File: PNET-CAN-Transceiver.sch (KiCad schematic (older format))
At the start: 14 parts, among them J301 Termination, J302 PNET, J303 PNET, U301 LM358, U302 TCAN332DR

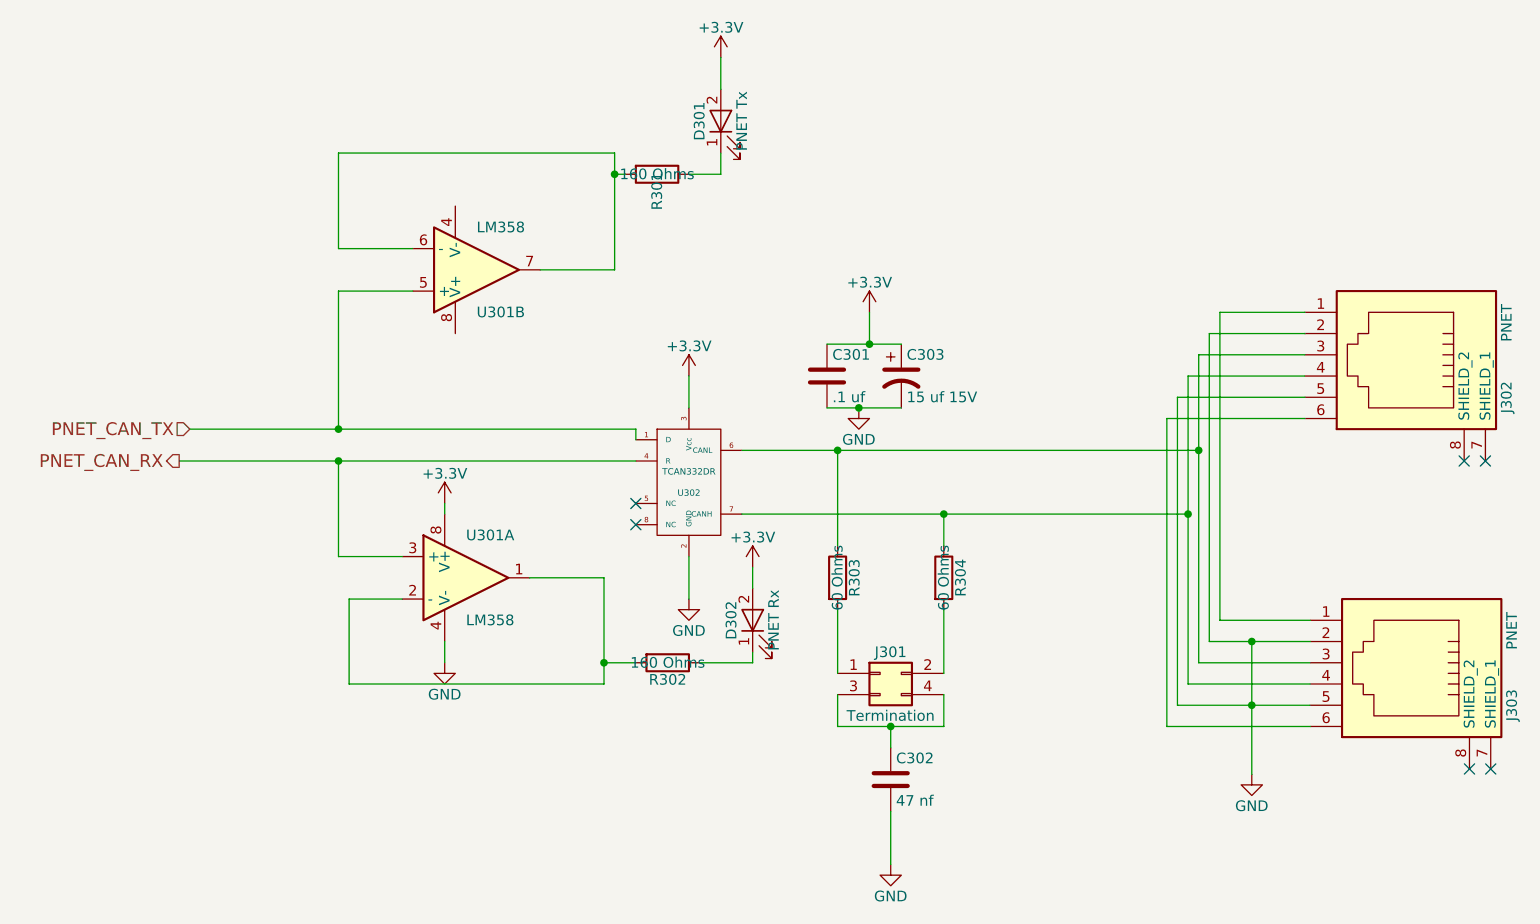
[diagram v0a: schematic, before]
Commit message: Correct for CAN Polarity on the PNET connectors.
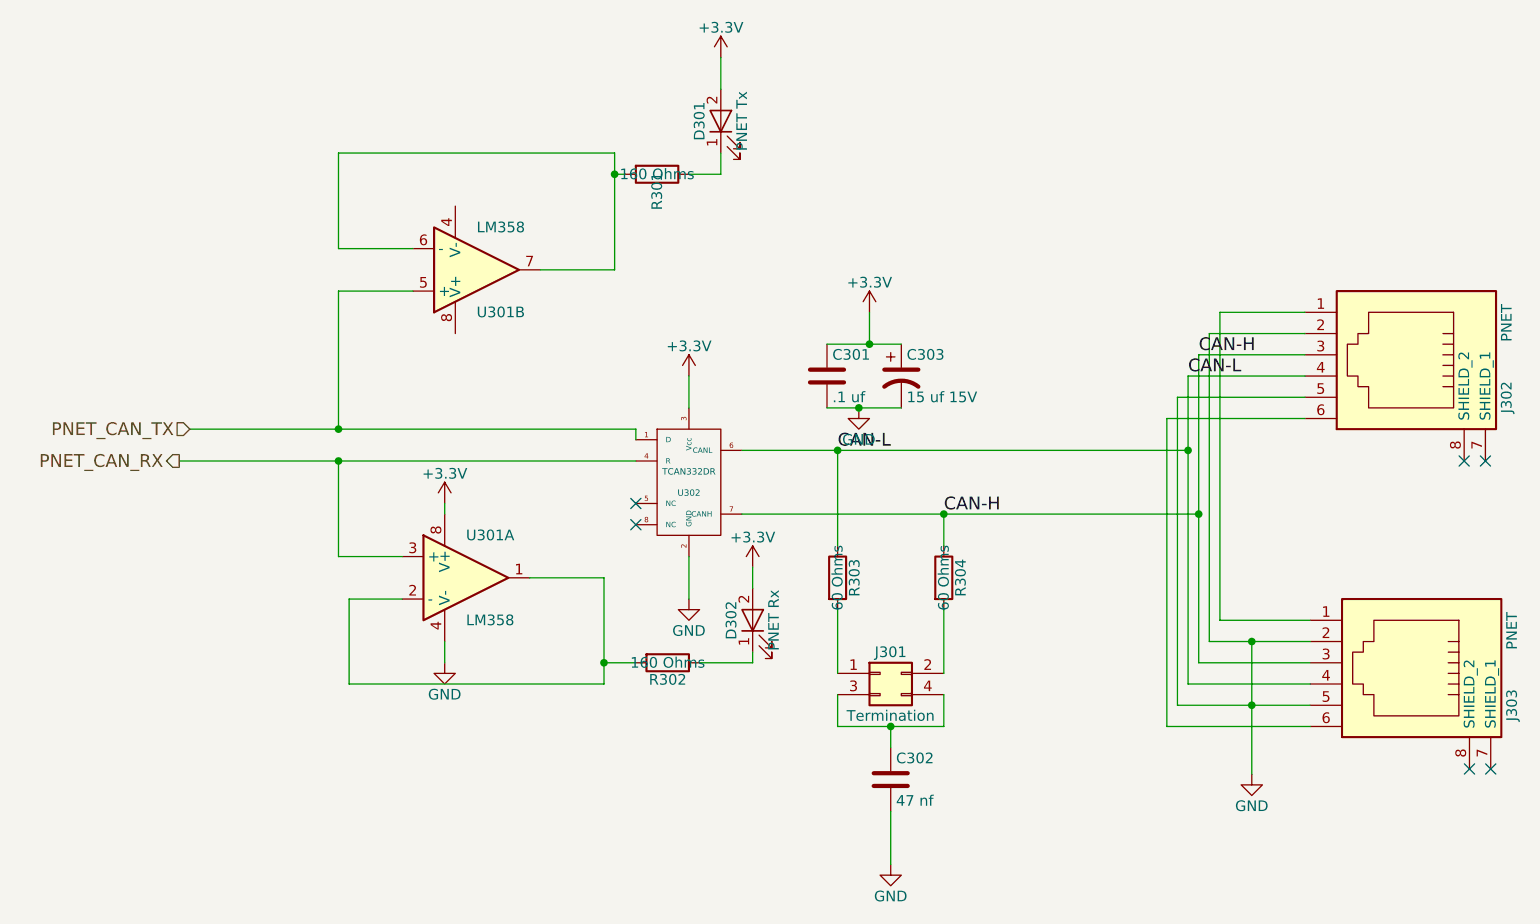
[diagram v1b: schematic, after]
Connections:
- net CAN-H: now reaches J302.3, J303.3
- net CAN-H: now also R304.1, U302.7 (CANH); no longer R303.1, U302.6 (CANL)
- net CAN-L: now reaches J302.4, J303.4
- net CAN-L: now also R303.1, U302.6 (CANL); no longer R304.1, U302.7 (CANH)
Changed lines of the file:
@@
 	7100 2150 7100 3600
 Wire Wire Line
-	7000 3800 7000 2350
+	7000 2350 7000 3100
 Wire Wire Line
-	6950 3900 6950 2450
+	7000 3100 7000 3800
+Wire Wire Line
+	6950 2450 6950 2800
+Wire Wire Line
+	6950 2800 6950 3900
 Wire Wire Line
 	6900 2550 6900 4000
@@
 Wire Wire Line
 	5300 3250 5300 2800
-Connection ~ 5300 2800
 Wire Wire Line
 	5800 3250 5800 3100
-Connection ~ 5800 3100
 Wire Wire Line
 	5300 3550 5300 3850
@@
 	5300 3950 5300 4100
 Wire Wire Line
-	5300 4100 5800 4100
+	5300 4100 5550 4100
+Wire Wire Line
+	5550 4100 5800 4100
 Wire Wire Line
 	5800 4100 5800 3950
@@
 	5550 4750 5550 4500
 Wire Wire Line
-	5250 2600 5600 2600
+	5250 2600 5400 2600
+Wire Wire Line
+	5400 2600 5600 2600
 Connection ~ 5400 2600
 Wire Wire Line
-	5250 2300 5600 2300
+	5250 2300 5450 2300
+Wire Wire Line
+	5450 2300 5600 2300
 Wire Wire Line
 	5450 2150 5450 2300
 Connection ~ 5450 2300
 Wire Wire Line
-	2250 2700 4350 2700
+	2250 2700 2950 2700
+Wire Wire Line
+	2950 2700 4350 2700
 Wire Wire Line
 	4350 2700 4350 2750
 Wire Wire Line
-	2200 2850 4350 2850
+	2200 2850 2950 2850
+Wire Wire Line
+	2950 2850 4350 2850
 Wire Wire Line
 	3250 3300 2950 3300
@@
 	3000 3500 3000 3900
 Wire Wire Line
-	3000 3900 4200 3900
+	4200 3900 3000 3900
 Wire Wire Line
-	4200 3900 4200 3400
+	4200 3400 4200 3800
+Wire Wire Line
+	4200 3800 4200 3900
 Wire Wire Line
 	4200 3400 3850 3400
@@
 	2950 1400 4250 1400
 Wire Wire Line
-	4250 1400 4250 1950
+	4250 1400 4250 1500
+Wire Wire Line
+	4250 1500 4250 1950
 Wire Wire Line
 	4250 1950 3900 1950
@@
 	7100 3600 7525 3600
 Wire Wire Line
-	7050 3700 7525 3700
+	7050 3700 7250 3700
 Wire Wire Line
-	7525 3800 7000 3800
+	7250 3700 7525 3700
 Wire Wire Line
-	7525 3900 6950 3900
+	7000 3800 7525 3800
 Wire Wire Line
-	6900 4000 7525 4000
+	6950 3900 7525 3900
+Wire Wire Line
+	6900 4000 7250 4000
+Wire Wire Line
+	7250 4000 7525 4000
 Wire Wire Line
 	7525 4100 6850 4100
@@
 	6850 2650 7500 2650
 Wire Wire Line
-	4850 2800 7000 2800
+	7250 3700 7250 4000
 Wire Wire Line
-	4850 3100 6950 3100
-Connection ~ 7000 2800
-Connection ~ 6950 3100
-Wire Wire Line
-	7250 3700 7250 4325
+	7250 4000 7250 4325
 Connection ~ 7250 4000
 Connection ~ 7250 3700
@@
 	1    0    0    -1
 $EndComp
+Wire Wire Line
+	4850 2800 5300 2800
+Wire Wire Line
+	5300 2800 6950 2800
+Text Label 7000 2350 0    60   ~ 0
+CAN-H
+Text Label 6950 2450 0    60   ~ 0
+CAN-L
+Wire Wire Line
+	4850 3100 5800 3100
+Wire Wire Line
+	5800 3100 7000 3100
+Text Label 5800 3100 0    60   ~ 0
+CAN-H
+Text Label 5300 2800 0    60   ~ 0
+CAN-L
+Connection ~ 6950 2800
+Connection ~ 5300 2800
+Wire Wire Line
+	7000 3100 7000 3100
+Connection ~ 7000 3100
+Connection ~ 5800 3100
 $EndSCHEMATC

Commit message: Correct for CAN Polarity on the PNET connectors.
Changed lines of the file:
@@
 	7100 2150 7100 3600
 Wire Wire Line
-	7000 2350 7000 3100
+	7000 2350 7000 3800
 Wire Wire Line
-	7000 3100 7000 3800
-Wire Wire Line
-	6950 2450 6950 2800
-Wire Wire Line
-	6950 2800 6950 3900
+	6950 2450 6950 3900
 Wire Wire Line
 	6900 2550 6900 4000
@@
 	5300 3950 5300 4100
 Wire Wire Line
-	5300 4100 5550 4100
-Wire Wire Line
-	5550 4100 5800 4100
+	5300 4100 5800 4100
 Wire Wire Line
 	5800 4100 5800 3950
@@
 	5550 4750 5550 4500
 Wire Wire Line
-	5250 2600 5400 2600
-Wire Wire Line
-	5400 2600 5600 2600
+	5250 2600 5600 2600
 Connection ~ 5400 2600
 Wire Wire Line
-	5250 2300 5450 2300
-Wire Wire Line
-	5450 2300 5600 2300
+	5250 2300 5600 2300
 Wire Wire Line
 	5450 2150 5450 2300
 Connection ~ 5450 2300
 Wire Wire Line
-	2250 2700 2950 2700
-Wire Wire Line
-	2950 2700 4350 2700
+	2250 2700 4350 2700
 Wire Wire Line
 	4350 2700 4350 2750
 Wire Wire Line
-	2200 2850 2950 2850
-Wire Wire Line
-	2950 2850 4350 2850
+	2200 2850 4350 2850
 Wire Wire Line
 	3250 3300 2950 3300
@@
 	4200 3900 3000 3900
 Wire Wire Line
-	4200 3400 4200 3800
-Wire Wire Line
-	4200 3800 4200 3900
+	4200 3400 4200 3900
 Wire Wire Line
 	4200 3400 3850 3400
@@
 	2950 1400 4250 1400
 Wire Wire Line
-	4250 1400 4250 1500
-Wire Wire Line
-	4250 1500 4250 1950
+	4250 1400 4250 1950
 Wire Wire Line
 	4250 1950 3900 1950
@@
 	7100 3600 7525 3600
 Wire Wire Line
-	7050 3700 7250 3700
-Wire Wire Line
-	7250 3700 7525 3700
+	7050 3700 7525 3700
 Wire Wire Line
 	7000 3800 7525 3800
@@
 	6950 3900 7525 3900
 Wire Wire Line
-	6900 4000 7250 4000
-Wire Wire Line
-	7250 4000 7525 4000
+	6900 4000 7525 4000
 Wire Wire Line
 	7525 4100 6850 4100
@@
 	6850 2650 7500 2650
 Wire Wire Line
-	7250 3700 7250 4000
-Wire Wire Line
-	7250 4000 7250 4325
+	7250 3700 7250 4325
 Connection ~ 7250 4000
 Connection ~ 7250 3700
@@
 $EndComp
 Wire Wire Line
-	4850 2800 5300 2800
-Wire Wire Line
-	5300 2800 6950 2800
+	4850 2800 6950 2800
 Text Label 7000 2350 0    60   ~ 0
 CAN-H
@@
 CAN-L
 Wire Wire Line
-	4850 3100 5800 3100
-Wire Wire Line
-	5800 3100 7000 3100
+	4850 3100 7000 3100
 Text Label 5800 3100 0    60   ~ 0
 CAN-H
@@
 Connection ~ 6950 2800
 Connection ~ 5300 2800
-Wire Wire Line
-	7000 3100 7000 3100
 Connection ~ 7000 3100
 Connection ~ 5800 3100

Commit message: Update RJ12 Jacks.
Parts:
- J302, J303: footprint Connectors:RJ12_E -> RJ12Molex:95501-2661; Mouser Part Number (none) -> 538-95501-2661
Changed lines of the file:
@@
 F 0 "J302" H 8150 2850 50  0000 C CNN
 F 1 "PNET" H 7800 2850 50  0000 C CNN
-F 2 "Connectors:RJ12_E" H 7950 2350 50  0001 C CNN
+F 2 "RJ12Molex:95501-2661" H 7950 2350 50  0001 C CNN
 F 3 "" H 7950 2350 50  0001 C CNN
+F 4 "538-95501-2661 " H 7950 2350 60  0001 C CNN "Mouser Part Number"
 	1    7950 2350
 	0    1    1    0
@@
 F 0 "J303" H 8175 4300 50  0000 C CNN
 F 1 "PNET" H 7825 4300 50  0000 C CNN
-F 2 "Connectors:RJ12_E" H 7975 3800 50  0001 C CNN
+F 2 "RJ12Molex:95501-2661" H 7975 3800 50  0001 C CNN
 F 3 "" H 7975 3800 50  0001 C CNN
+F 4 "538-95501-2661 " H 7975 3800 60  0001 C CNN "Mouser Part Number"
 	1    7975 3800
 	0    1    1    0
@@
 	3000 3500 3000 3900
 Wire Wire Line
-	4200 3900 3000 3900
+	3000 3900 4200 3900
 Wire Wire Line
-	4200 3400 4200 3900
+	4200 3900 4200 3400
 Wire Wire Line
 	4200 3400 3850 3400
